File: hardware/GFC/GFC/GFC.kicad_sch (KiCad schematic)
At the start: 9 parts, among them J2 Pi Zero/Zero W, Q1 Q_NPN_BCE, T1 DS18B20 - Connector, T2 DS18B20 - Connector, T3 DS18B20 - Connector, U2 LTV-356T

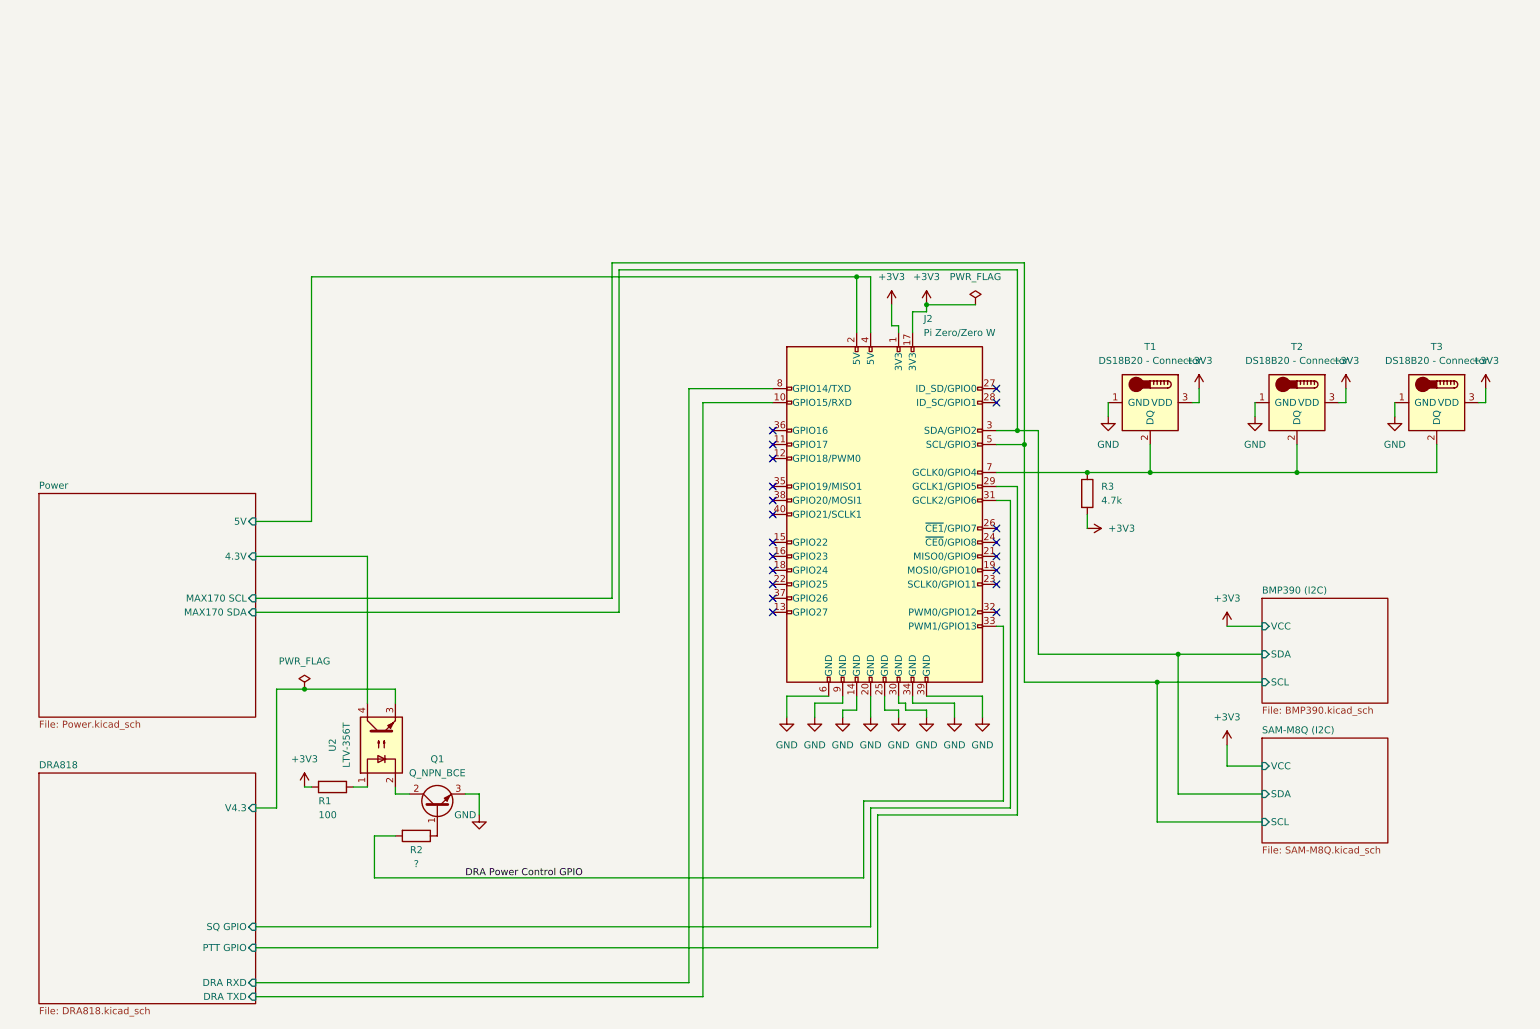
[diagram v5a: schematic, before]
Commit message: Schematic Update - ADC/DAC & GPIO Config EEPROM
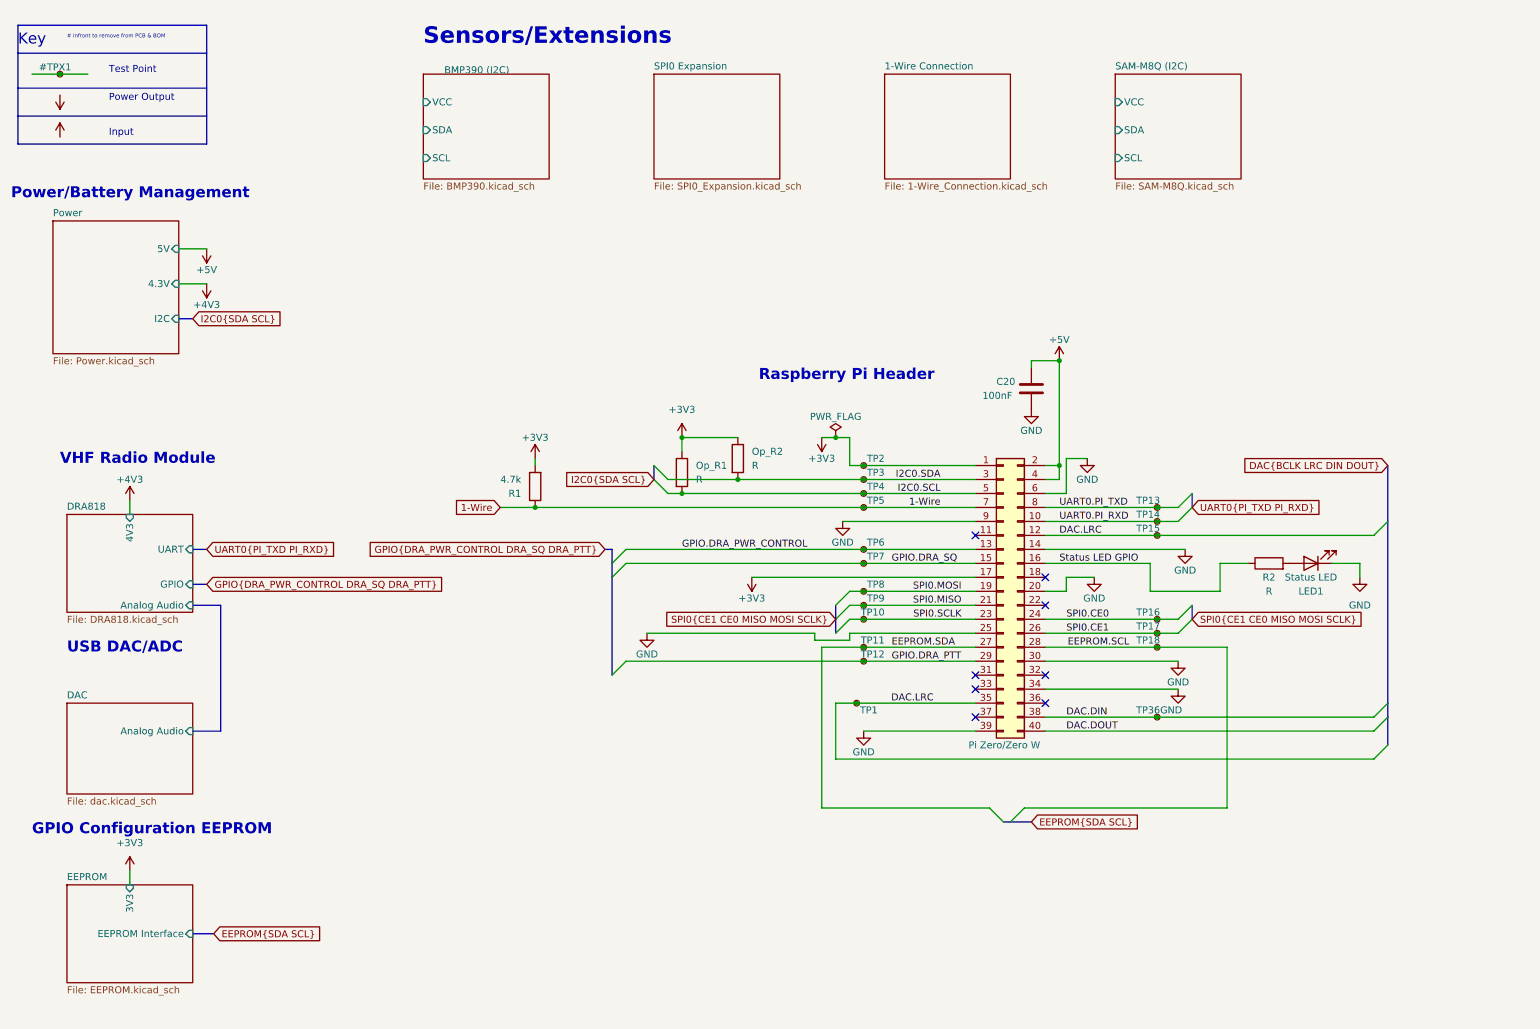
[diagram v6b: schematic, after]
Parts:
- removed Q1: Q_NPN_BCE, Package_TO_SOT_SMD:SOT-23, symbol Device:Q_NPN_BCE
- removed R3: 4.7k, Resistor_SMD:R_0603_1608Metric_Pad0.98x0.95mm_HandSolder, symbol Device:R
- removed T1, T2, T3: DS18B20 - Connector, Connector_JST:JST_XH_B3B-XH-AM_1x03_P2.50mm_Vertical, symbol Sensor_Temperature:DS18B20
- removed U2: LTV-356T, Package_SO:SO-4_4.4x3.6mm_P2.54mm, symbol Isolator:LTV-356T
- added C20: 100nF, symbol Device:C
- added LED1: Status LED, symbol Device:LED
- added Op_R1, Op_R2: R, symbol Device:R
- added TP1, TP10, TP11, TP12, TP13, TP14, TP15, TP16, TP17, TP18, TP2, TP3, TP36, TP4, TP5, TP6, TP7, TP8, TP9: Test Point, symbol Connector:TestPoint_Small
- CPU1: renamed from J2; symbol Connector:Raspberry_Pi_2_3 -> Connector_Generic:Conn_02x20_Odd_Even
- R1: value 100 -> 4.7k; footprint Resistor_SMD:R_0805_2012Metric_Pad1.20x1.40mm_HandSolder -> Resistor_SMD:R_0603_1608Metric_Pad0.98x0.95mm_HandSolder; Digikey https://www.digikey.com/short/j2drdv0p -> https://www.digikey.com/short/m931v8f8; Min Wat 0.036 -> (none)
- R2: value ? -> R; footprint Resistor_SMD:R_0603_1608Metric_Pad0.98x0.95mm_HandSolder -> (none); Digikey ? -> (none)
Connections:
- net +3V3: now also Op_R1.1, Op_R2.1, TP2.1
- net BMP390 (I2C)/SCL: no longer CPU1.5 (SCL/GPIO3)
- net BMP390 (I2C)/SDA: no longer CPU1.3 (SDA/GPIO2)
- net GND: now also C20.2, LED1.1 (K)
- net 1-Wire: now reaches R1.1
- net 1-Wire: now also CPU1.7 (Pin_7), TP5.1
- net Status LED GPIO: now reaches R2.1
- net Status LED GPIO: now also CPU1.16 (Pin_16)
- net DAC.LRC: now reaches CPU1.12 (Pin_12)
- net DAC.LRC: now also CPU1.35 (Pin_35), TP1.1, TP15.1
- net GPIO.DRA_PWR_CONTROL: now reaches CPU1.13 (Pin_13)
- net GPIO.DRA_PWR_CONTROL: now also TP6.1
- net GPIO.DRA_SQ: now reaches CPU1.15 (Pin_15)
- net GPIO.DRA_SQ: now also TP7.1
- net SPI0.MOSI: now reaches CPU1.19 (Pin_19)
- net SPI0.MOSI: now also TP8.1
- net SPI0.MISO: now reaches CPU1.21 (Pin_21)
- net SPI0.MISO: now also TP9.1
- net SPI0.SCLK: now reaches CPU1.23 (Pin_23)
- net SPI0.SCLK: now also TP10.1
- net SPI0.CE0: now reaches CPU1.24 (Pin_24)
- net SPI0.CE0: now also TP16.1
- net SPI0.CE1: now reaches CPU1.26 (Pin_26)
- net SPI0.CE1: now also TP17.1
- net EEPROM.SDA: now reaches CPU1.27 (Pin_27)
- net EEPROM.SDA: now also TP11.1
- net EEPROM.SCL: now reaches CPU1.28 (Pin_28)
- net EEPROM.SCL: now also TP18.1
- net DAC.DIN: now reaches CPU1.38 (Pin_38)
- net DAC.DIN: now also TP36.1
- net DAC.DOUT: now reaches CPU1.40 (Pin_40)
- net DRA Power Control GPIO: no longer names the net of R2.2
- net DRA Power Control GPIO: now also LED1.2 (A); no longer CPU1.33 (PWM1/GPIO13)
- net DRA818/DRA RXD renamed UART0.PI_TXD
- net UART0.PI_TXD: now also TP13.1
- net DRA818/DRA TXD renamed UART0.PI_RXD
- net UART0.PI_RXD: now also TP14.1
- net DRA818/PTT GPIO renamed GPIO.DRA_PTT
- net GPIO.DRA_PTT: now also TP12.1
- net DRA818/SQ GPIO: no longer names the net of CPU1.31 (Pin_31)
- net Power/5V renamed +5V
- net +5V: now also C20.1
- new net I2C0.SCL: CPU1.5 (Pin_5), Op_R1.2, TP4.1
- new net I2C0.SDA: CPU1.3 (Pin_3), Op_R2.2, TP3.1
- no-connect marks 20 -> 8
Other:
- added sheet 1-Wire Connection (1-Wire_Connection.kicad_sch)
- added sheet DAC (dac.kicad_sch)
- added sheet EEPROM (EEPROM.kicad_sch)
- added sheet SPI0 Expansion (SPI0_Expansion.kicad_sch)
- sheet DRA818 ports: added 4V3, Analog Audio, GPIO, UART; removed DRA RXD, DRA TXD, PTT GPIO, SQ GPIO, V4.3
- sheet Power ports: added I2C; removed MAX170 SCL, MAX170 SDA
- note added: "# infront to remove from PCB & BOM"
- note added: "GPIO Configuration EEPROM"
- note added: "Input"
- note added: "Key"
- note added: "Power Output"
- note added: "Power/Battery Management"
- note added: "Raspberry Pi Header"
- note added: "Sensors/Extensions"
- note added: "Test Point"
- note added: "USB DAC/ADC"
- note added: "VHF Radio Module"

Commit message: sync
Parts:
- removed TP1, TP36: Test Point, symbol Connector:TestPoint_Small
- TP10, TP11, TP12, TP13, TP14, TP15, TP16, TP17, TP18, TP2, TP3, TP4, TP5, TP6, TP7, TP8, TP9: footprint (none) -> TestPoint:TestPoint_Pad_D1.0mm
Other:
- sheet 1-Wire Connection ports: added 1-Wire, VCC; removed none
- sheet BMP390 (I2C) ports: added I2C{SDA SCL}; removed SCL, SDA
- sheet DAC ports: added AUDIO{SC_IN_L SC_IN_R SC_OUT_L SC_OUT_R}, DAC{BCLK LRC DIN DOUT}; removed Analog Audio
- sheet DRA818 ports: added AUDIO{SC_IN_L SC_IN_R SC_OUT_L SC_OUT_R}, GPIO{DRA_PWR_CONTROL DRA_SQ DRA_PTT}, UART0{PI_TXD PI_RXD}; removed Analog Audio, GPIO, UART
- sheet EEPROM ports: added EEPROM{SDA SCL}; removed EEPROM Interface
- sheet Power ports: added I2C0{SDA SCL}; removed I2C
- sheet SAM-M8Q (I2C) ports: added I2C0{SDA SCL}; removed SCL, SDA
- sheet SPI0 Expansion ports: added SPI0{CE1 CE0 MISO MOSI SCLK}, VCC; removed none
- note removed: "# infront to remove from PCB & BOM"
- note removed: "Input"
- note removed: "Key"
- note removed: "Power Output"
- note removed: "Test Point"
